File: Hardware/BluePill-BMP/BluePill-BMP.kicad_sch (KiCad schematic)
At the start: 23 parts, among them J1 Conn_01x07, J2 Conn_01x05, J3 Conn_01x11, J4 GDB_COMM, J5 VCC, J6 GND, J7 JTAG, J8 LogicAna, U1 FT232RL_Breakout, U2 STM32F103 BluePill

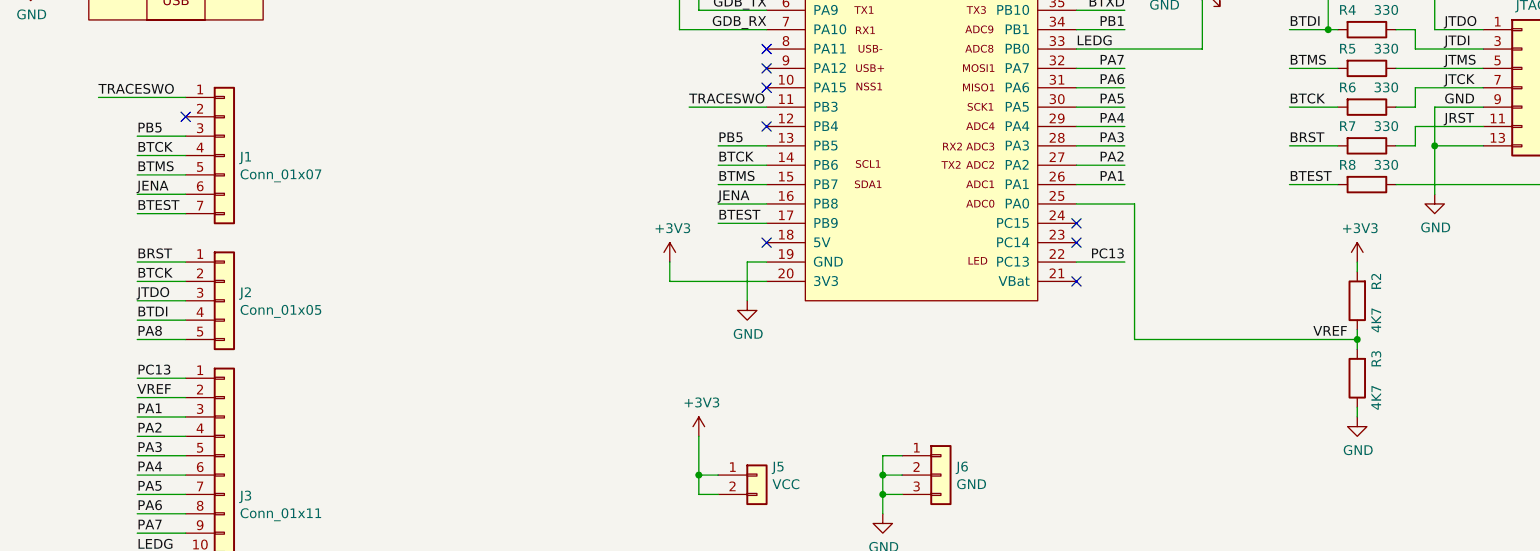
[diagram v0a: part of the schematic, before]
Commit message: BluePill Hardware: Swapped TIM4 Ch1 and Ch2 (reversed input and output) ass Ch2 input produces less delay, besides, simultaneous DMA access to the SPI2 is also possible.
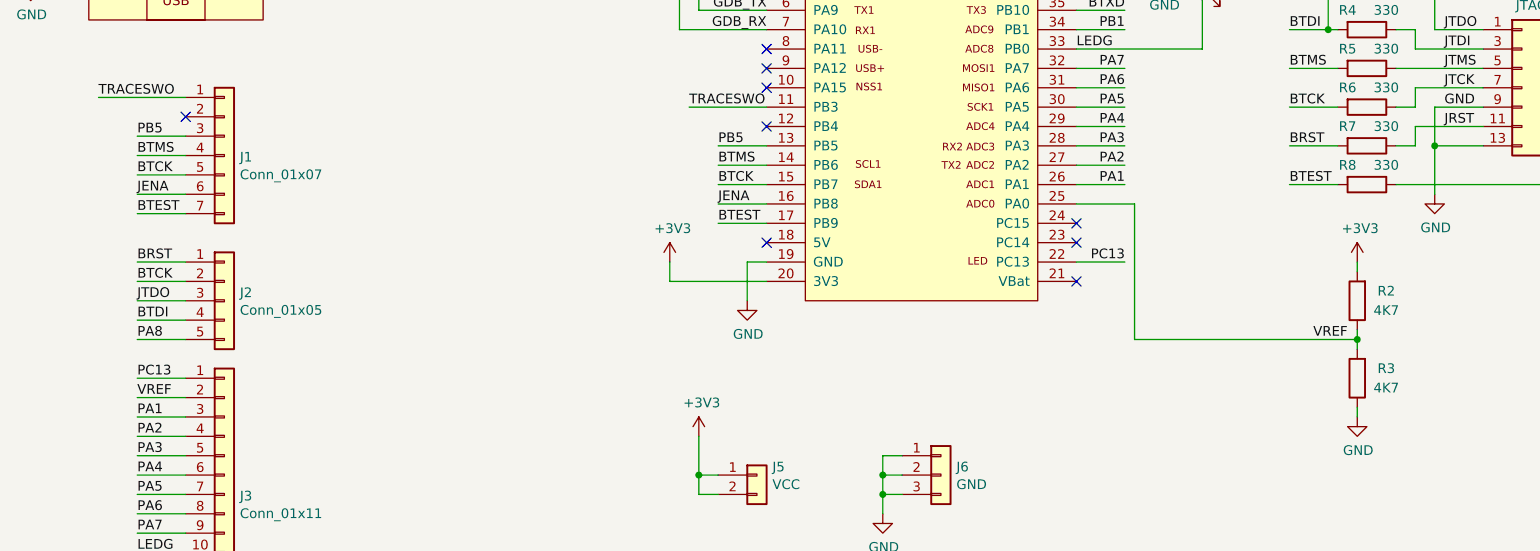
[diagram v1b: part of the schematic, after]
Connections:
- net BTCK: now also J1.5 (Pin_5), U2.15 (PB7); no longer J1.4 (Pin_4), U2.14 (PB6)
- net BTMS: now also J1.4 (Pin_4), U2.14 (PB6); no longer J1.5 (Pin_5), U2.15 (PB7)
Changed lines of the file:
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@@
   (title_block
     (title "MSPBMP Development Protoboard")
-    (date "2021-12-04")
-    (rev "2")
+    (date "2022-01-09")
+    (rev "3")
     (company "Mathias Gruber")
     (comment 1 "With optional TRACE SWO using FT232RL")
@@
     (effects (font (size 1.27 1.27)) (justify right bottom))
   )
-  (label "BTCK" (at 41.91 104.14 0)
+  (label "BTCK" (at 41.91 106.68 0)
     (effects (font (size 1.27 1.27)) (justify left bottom))
   )
@@
     (effects (font (size 1.27 1.27)) (justify left bottom))
   )
-  (label "BTMS" (at 118.11 107.95 0)
+  (label "BTMS" (at 118.11 105.41 0)
     (effects (font (size 1.27 1.27)) (justify left bottom))
   )
@@
     (effects (font (size 1.27 1.27)) (justify right bottom))
   )
-  (label "BTMS" (at 41.91 106.68 0)
+  (label "BTMS" (at 41.91 104.14 0)
     (effects (font (size 1.27 1.27)) (justify left bottom))
   )
@@
     (effects (font (size 1.27 1.27)) (justify left bottom))
   )
-  (label "BTCK" (at 118.11 105.41 0)
+  (label "BTCK" (at 118.11 107.95 0)
     (effects (font (size 1.27 1.27)) (justify left bottom))
   )
@@
   (symbol (lib_id "Device:R") (at 201.93 123.19 180) (unit 1)
     (in_bom yes) (on_board yes)
-    (property "Reference" "R2" (id 0) (at 204.47 120.65 90))
-    (property "Value" "4K7" (id 1) (at 204.47 125.73 90))
+    (property "Reference" "R2" (id 0) (at 205.74 121.92 0))
+    (property "Value" "4K7" (id 1) (at 205.74 124.46 0))
     (property "Footprint" "Resistor_THT:R_Axial_DIN0204_L3.6mm_D1.6mm_P7.62mm_Horizontal" (id 2) (at 203.708 123.19 90)
       (effects (font (size 1.27 1.27)) hide)
@@
   (symbol (lib_id "Device:R") (at 201.93 133.35 180) (unit 1)
     (in_bom yes) (on_board yes)
-    (property "Reference" "R3" (id 0) (at 204.47 130.81 90))
-    (property "Value" "4K7" (id 1) (at 204.47 135.89 90))
+    (property "Reference" "R3" (id 0) (at 205.74 132.08 0))
+    (property "Value" "4K7" (id 1) (at 205.74 134.62 0))
     (property "Footprint" "Resistor_THT:R_Axial_DIN0204_L3.6mm_D1.6mm_P7.62mm_Horizontal" (id 2) (at 203.708 133.35 90)
       (effects (font (size 1.27 1.27)) hide)
